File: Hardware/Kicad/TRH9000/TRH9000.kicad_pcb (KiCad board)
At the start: 4 copper layers, 99.1 x 66.6 mm, 89 parts, among them J1 Norcomp_200-015-263R001, J2 Console5_SCART, Q1 BC817, U1 V9990, U2 KM428C256, U3 KM428C256, U4 74VHC138, U5 T.I_SN74AHCT32D, U6 LMH1980, X1 Crystek_CE3291, Y1 Y_HCM4921477270ABJT

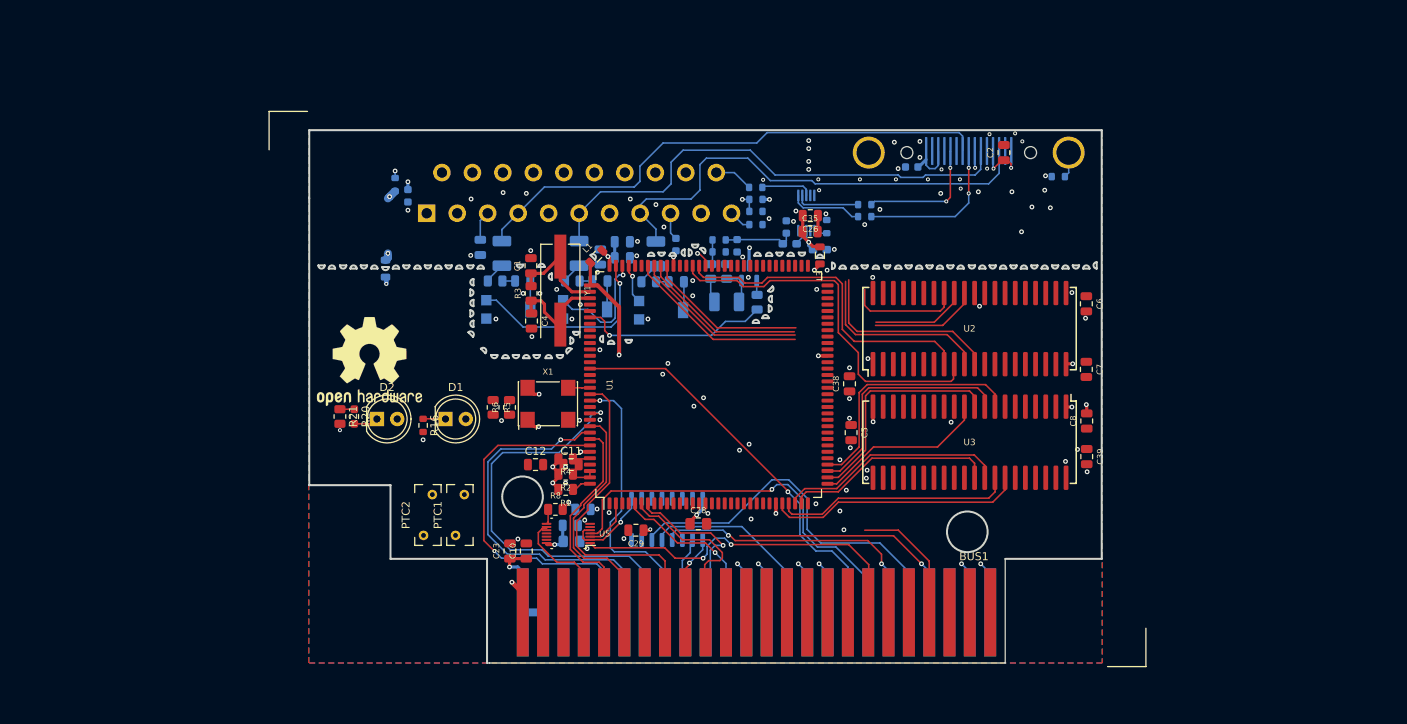
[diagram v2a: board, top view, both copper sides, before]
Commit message: Did a reroute of the analog / digital separation.
Did a reroute of the analog / digital separation.
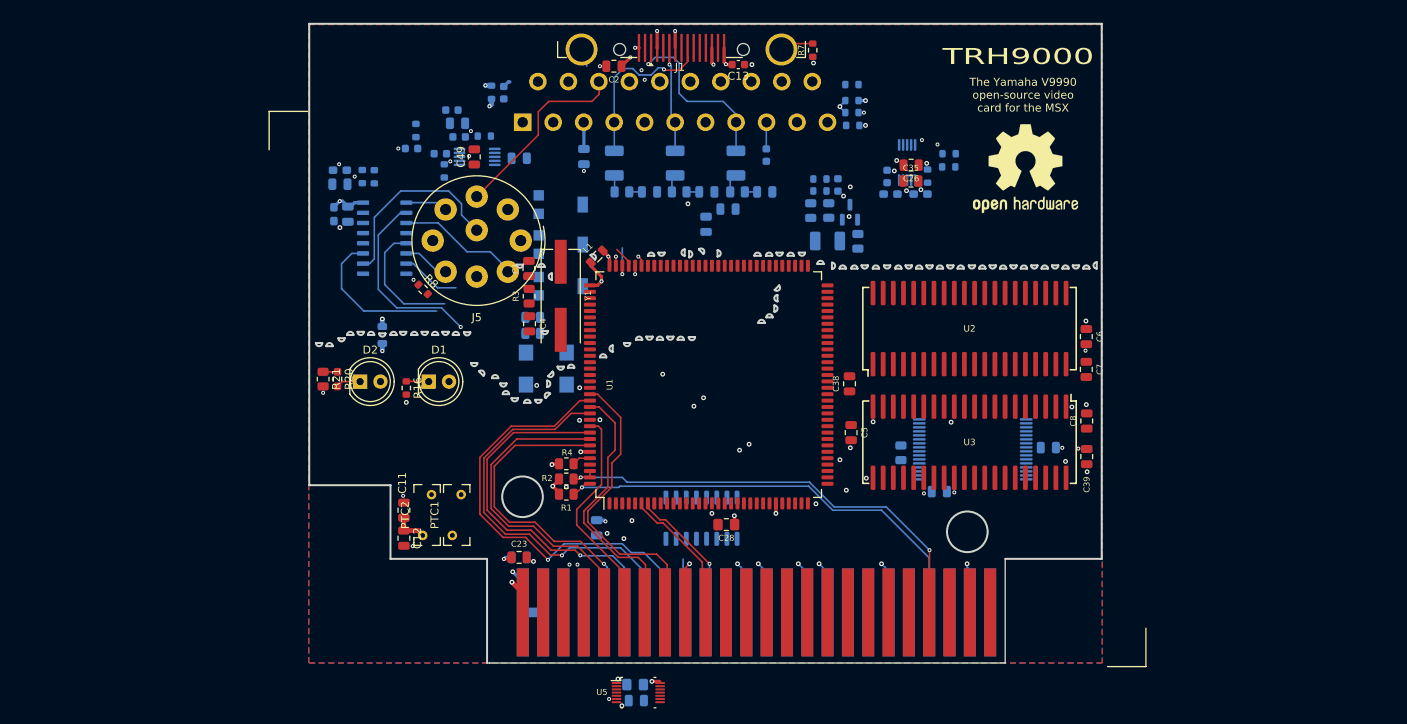
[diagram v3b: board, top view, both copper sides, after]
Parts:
- removed L3: L_MLZ2012M4R7HT000, Inductor_SMD:L_0805_2012Metric
- added C18: C_CL10B104KB8NNNL, Capacitor_SMD:C_0603_1608Metric_Pad1.08x0.95mm_HandSolder, B.Cu at (101.3, 70.9)
- added C22: 47pF, Capacitor_SMD:C_0603_1608Metric, B.Cu at (117.0, 61.2)
- added C41: C_CC0805JPX7R9BB104, Capacitor_SMD:C_0805_2012Metric, B.Cu at (116.8, 59.5)
- added C42: 47pF, Capacitor_SMD:C_0603_1608Metric, B.Cu at (111.0, 62.7)
- added C43: 47pF, LRJ:C_0603_1608Metric_round_court, B.Cu at (116.1, 57.9)
- added C44: C_CL10B104KB8NNNL, LRJ:C_0603_1608Metric_round_court, B.Cu at (114.7, 63.3)
- added C45: C_CL21B106KOQNNNE, Capacitor_SMD:C_0805_2012Metric, B.Cu at (190.7, 100.1)
- added C46: C_CC0805JPX7R9BB104, Capacitor_SMD:C_0805_2012Metric, B.Cu at (177.0, 105.6)
- added C47: C_CL21B106KOQNNNE, Capacitor_SMD:C_0805_2012Metric, B.Cu at (102.1, 67.2)
- added C48: C_CL10B104KB8NNNL, Capacitor_SMD:C_0603_1608Metric_Pad1.08x0.95mm_HandSolder, B.Cu at (102.1, 65.4)
- added C49: 10nF, Capacitor_SMD:C_0805_2012Metric, F.Cu at (118.9, 63.7)
- added J5: DIN-8_SD-80BV, LRJ:Jack_DIN_CUI_SD-80BV_Vertical, F.Cu at (119.2, 74.2)
- added R22: 75, Resistor_SMD:R_0603_1608Metric, B.Cu at (120.2, 61.1)
- added R23: 100, LRJ:R_0603_1608Metric_roundcourt, B.Cu at (111.6, 60.4)
- added R30: R_RC0603FR-0710KL, LRJ:R_0603_1608Metric_roundcourt, B.Cu at (115.2, 65.5)
- added R31: 100, Resistor_SMD:R_0603_1608Metric, B.Cu at (106.4, 66.2)
- added R32: 100, Resistor_SMD:R_0603_1608Metric, B.Cu at (104.9, 66.2)
- added R34: 4K7, Resistor_SMD:R_0805_2012Metric, B.Cu at (172.2, 100.7)
- added U7: T.I_SN74CBT3257, trh9000:Texas_R-PDSO-G16_3.9x9.9mm, B.Cu at (107.7, 73.9)
- added U8: LMH1980, Package_SO:VSSOP-10_3x3mm_P0.5mm, B.Cu at (119.2, 63.7)
- added U9: SST39SF010A-lrj, Package_SO:TSOP-I-32_12.4x8mm_P0.5mm, B.Cu at (181.2, 100.3)
- C10, C29, R5, R6, X1: moved to B.Cu
- C13, J1, R7: moved to F.Cu
- C9: value 47pF -> C_CL21B106KOQNNNE
- R8: value 2K2 -> R_ERJ-3GEYJ105V; footprint Resistor_SMD:R_0805_2012Metric -> Resistor_SMD:R_0603_1608Metric
- moved LOGO1 85.5 mm to (187.8, 65.2)
- moved C2 49.9 mm to (136.3, 52.4), turned to 180 degrees
- moved C9 47.2 mm to (103.1, 70.9), turned to -90 degrees
- moved J1 38.1 mm to (144.8, 46.9), turned to 180 degrees
- moved R7 34.5 mm to (161.2, 50.4), turned to 90 degrees
- moved R8 32.1 mm to (112.5, 80.3), turned to -45 degrees
- moved C13 25.2 mm to (151.9, 52.2), turned to 180 degrees
- moved C31 23.4 mm to (139.2, 131.7), turned to 180 degrees
- moved U5 21.7 mm to (139.4, 130.7), turned to 0 degrees
- moved C11 21.7 mm to (110.1, 107.9), turned to 90 degrees
- moved C30 19.6 mm to (139.0, 129.7), turned to 180 degrees
- moved C16 19.4 mm to (140.8, 68.1)
- moved R19 19.4 mm to (137.3, 68.1)
- moved C12 18.8 mm to (110.1, 111.4), turned to -90 degrees
- moved RV1 18.2 mm to (129.7, 69.7)
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- renumbered C37 to locked
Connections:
- net /VDP/HRESET renamed /V9958_HSYNC
- net /VDP/VRESET renamed /V9958_VSYNC
- net /VDP/~{CSYNC} renamed /VDP/~{CSYNCi}
- net /VIDEO/REXT renamed /VIDEO/REXTi
- BUS1 pad 1: /~{CS1} -> unconnected-(BUS1-Pad1)
- BUS1 pad 12: /~{MERQ} -> unconnected-(BUS1-Pad12)
- BUS1 pad 2: /~{CS2} -> unconnected-(BUS1-Pad2)
- BUS1 pad 42: /SYS_CLK -> unconnected-(BUS1-Pad42)
- C9 pad 1: Net-(C9-Pad1) -> +5VA
- J2 pad 6: unconnected-(J2-Pad6) -> /SOUNDOUT
- R5 pad 1: +5VP -> +5VA
- R6 pad 2: +5VP -> +5VA
- R8 pad 1: Net-(C9-Pad1) -> GND
- R8 pad 2: /SCIN -> Net-(J5-PadSH)
- RV1 pad 3: /VDP/R -> /VIDEO/Rm
- RV2 pad 3: /VDP/G -> /VIDEO/Gm
- RV3 pad 3: /VDP/B -> /VIDEO/Bm
- U1 pad 10: unconnected-(U1-Pad10) -> /VDP/KA15
- U1 pad 11: unconnected-(U1-Pad11) -> /VDP/KA14
- U1 pad 12: unconnected-(U1-Pad12) -> /VDP/KA13
- U1 pad 13: unconnected-(U1-Pad13) -> /VDP/KA12
- U1 pad 14: unconnected-(U1-Pad14) -> /VDP/KA11
- U1 pad 15: unconnected-(U1-Pad15) -> /VDP/KA10
- U1 pad 16: unconnected-(U1-Pad16) -> /VDP/KA9
- U1 pad 37: unconnected-(U1-Pad37) -> /VDP/~{KOE}
- U1 pad 9: unconnected-(U1-Pad9) -> /VDP/KA16
- U1 pad 91: unconnected-(U1-Pad91) -> /VDP/~{YSi}
- U1 pad 93: /VDP/R -> /VDP/Ri
- U1 pad 94: /VDP/G -> /VDP/Gi
- U1 pad 95: /VDP/B -> /VDP/Bi
- U5 pad 10: /SYS_CLK -> unconnected-(U5-Pad10)
- U5 pad 8: /SCIN -> unconnected-(U5-Pad8)
- U5 pad 9: /SYS_CLK -> unconnected-(U5-Pad9)
- X1 pad 1: +5VP -> +5VA
- X1 pad 4: +5VP -> +5VA
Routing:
- net /~{WR}: track 50.8 -> 0.00 mm, vias 1 -> 0
- net /~{RESET}: track 50.5 -> 0.00 mm, vias 1 -> 0
- net /VIDEO/GOUT: track 62.7 -> 13.2 mm, vias 0 -> 1
- net /VDP/V1D1: track 48.3 -> 0.00 mm
- net /~{M1}: track 47.7 -> 0.00 mm
- net /VIDEO/BOUT: track 67.2 -> 20.7 mm, vias 0 -> 1
- net /~{RD}: track 44.6 -> 0.00 mm, vias 2 -> 0
- net /VDP/V1D0: track 41.1 -> 0.00 mm
- net /~{INT}: track 21.3 -> 58.1 mm, vias 0 -> 2
- net /VDP/V1D6: track 36.0 -> 0.00 mm
- net /VIDEO/ROUT: track 59.2 -> 23.2 mm, vias 0 -> 1
- net /D2: track 0.00 -> 34.0 mm
- net /VDP/V1D4: track 33.8 -> 0.00 mm
- net /VDP/V0D7: track 33.4 -> 0.00 mm
- net /VDP/V1D5: track 32.9 -> 0.00 mm
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- added copper zone on In1.Cu, net /VIDEO/GNDD
- added copper zone on In1.Cu, net /VIDEO/VGA_GND
- removed copper zone on In1.Cu, net /VIDEO/AUGND
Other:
- board size 99.1 x 66.6 mm -> 99.1 x 79.9 mm
- board text added: "TRH9000"
- board text removed: "TRH900"

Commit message: Restarted routing from scratch.
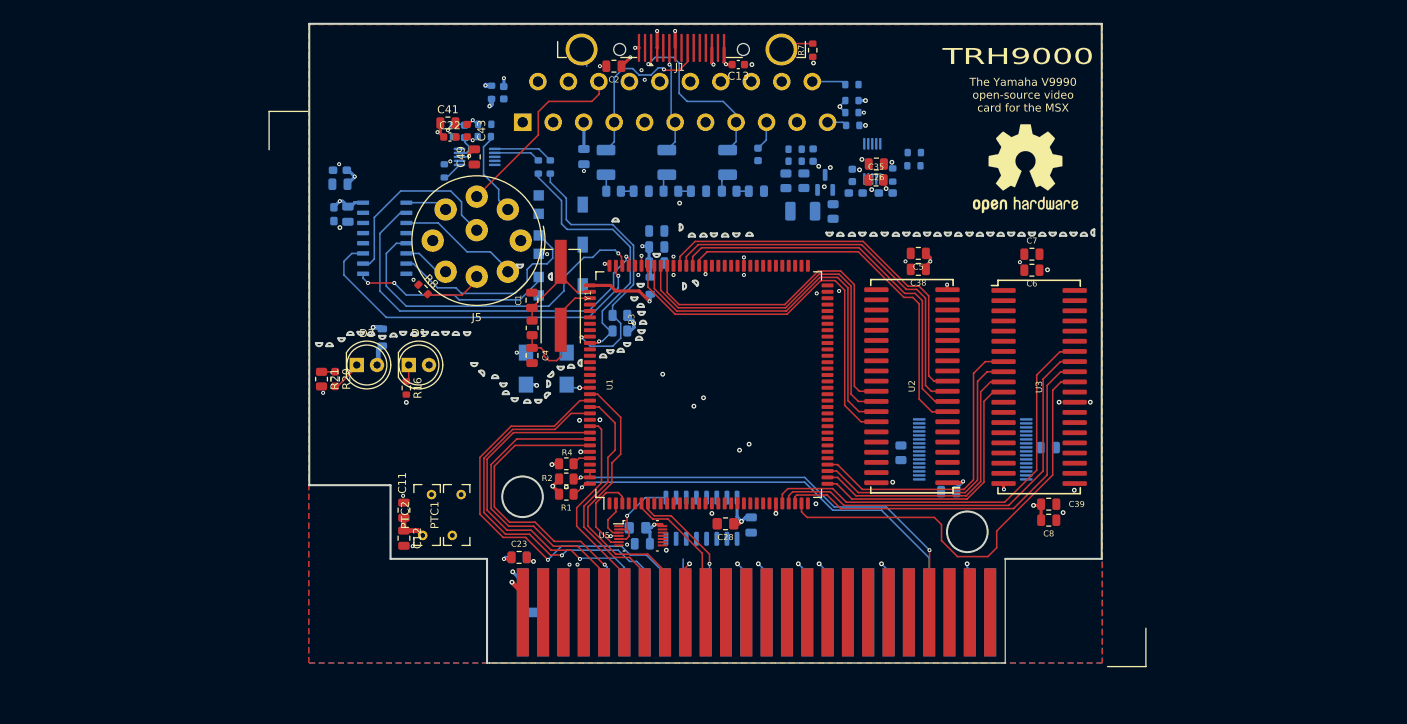
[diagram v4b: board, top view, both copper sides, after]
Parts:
- C22, C41, C43: moved to F.Cu
- L1: moved to B.Cu
- moved C5 23.9 mm to (174.4, 75.8), turned to 180 degrees
- moved R31 22.0 mm to (128.4, 65.0)
- moved R32 22.0 mm to (126.9, 65.0)
- moved C3 21.6 mm to (141.7, 77.0)
- moved C31 19.6 mm to (139.9, 112.1)
- moved C30 19.6 mm to (139.3, 110.1)
- moved U5 19.6 mm to (139.7, 111.1)
- moved C29 19.3 mm to (153.5, 109.8)
- moved C38 16.7 mm to (174.4, 77.8), turned to 180 degrees
- moved C7 15.9 mm to (188.6, 75.9), turned to 0 degrees
- moved C8 13.3 mm to (190.7, 109.2), turned to 180 degrees
- moved U3 11.1 mm to (189.5, 92.5), turned to 0 degrees
- moved R6 10.9 mm to (137.1, 85.5), turned to 0 degrees
- moved R5 10.9 mm to (137.1, 83.5), turned to 180 degrees
- moved C6 10.7 mm to (188.6, 77.9), turned to 180 degrees
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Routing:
- net /VDP/V0D4: track 0.00 -> 55.2 mm
- net /VDP/V0D7: track 0.00 -> 53.5 mm
- net /VDP/V0D6: track 0.00 -> 51.8 mm
- net /VDP/V0D5: track 0.00 -> 50.2 mm
- net /VDP/V1D7: track 0.00 -> 50.1 mm
- net /VDP/V1D6: track 0.00 -> 48.7 mm
- net /VDP/V1D3: track 0.00 -> 48.5 mm
- net /VDP/V1D2: track 0.00 -> 48.4 mm
- net /VDP/V1D1: track 0.00 -> 47.8 mm
- net /VDP/V1D0: track 0.00 -> 47.5 mm
- net /VDP/V1D5: track 0.00 -> 47.3 mm
- net /VDP/V1D4: track 0.00 -> 45.5 mm
- net /VDP/V0D0: track 0.00 -> 37.7 mm
- net /VDP/V0D1: track 0.00 -> 36.6 mm
- net /V9958_HSYNC: track 0.00 -> 36.3 mm, vias 0 -> 1
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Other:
- outline, holes or cut-outs redrawn

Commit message: Further routing, analog is almost complete.
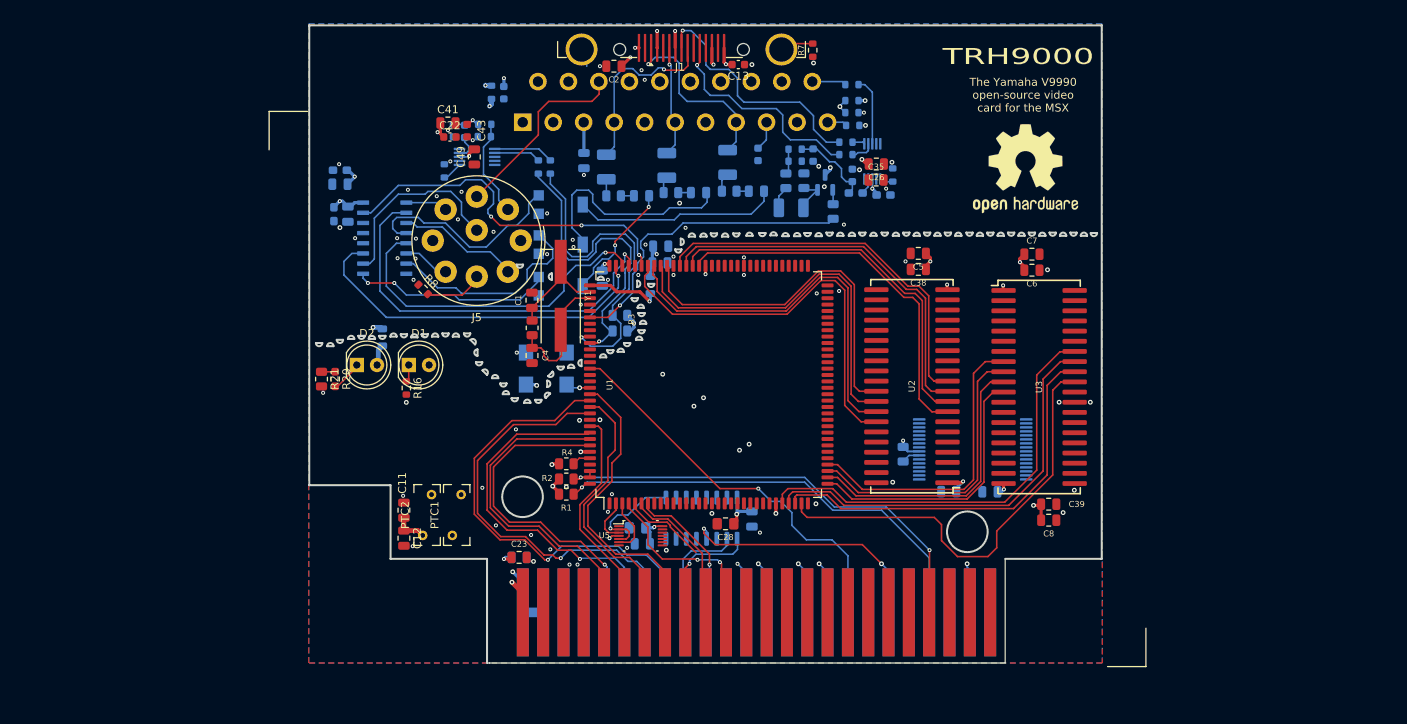
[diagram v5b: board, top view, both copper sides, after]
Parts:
- moved C45 9.16 mm to (183.3, 105.6)
- moved locked 9.00 mm to (134.9, 78.9), turned to -90 degrees
- moved R25 9.00 mm to (165.3, 61.9), turned to 0 degrees
- moved R26 8.55 mm to (165.3, 63.5), turned to 0 degrees
- moved C17 1.51 mm to (158.5, 70.1)
- moved C29 0.76 mm to (153.6, 109.0)
- moved C21 0.58 mm to (135.4, 65.0)
- moved C16 0.58 mm to (139.8, 68.6)
- moved R19 0.57 mm to (136.3, 68.6)
- moved C27 0.51 mm to (142.2, 74.9)
- moved C24 0.50 mm to (132.6, 64.2)
- moved C3 0.40 mm to (142.1, 77.0)
- moved C20 0.38 mm to (143.0, 64.8)
- moved C36 0.37 mm to (170.1, 68.5)
- moved R34 0.33 mm to (172.5, 100.9)
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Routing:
- net /~{RESET}: track 0.00 -> 50.0 mm, vias 0 -> 1
- net /VDP/~{YSi}: track 1.25 -> 45.2 mm, vias 1 -> 3
- net /VDP/~{CSYNCi}: track 0.00 -> 39.0 mm, vias 0 -> 1
- net /VIDEO/HSYNC: track 0.00 -> 31.3 mm, vias 0 -> 1
- net /VIDEO/GIN: track 0.00 -> 27.6 mm
- net /VIDEO/VSYNC: track 0.00 -> 27.2 mm, vias 0 -> 1
- net /VIDEO/Rm: track 0.00 -> 26.2 mm
- net /~{IORQ}: track 6.44 -> 32.2 mm, vias 1 -> 2
- net /VIDEO/RIN: track 0.00 -> 25.7 mm
- net /A0: track 0.00 -> 22.6 mm, vias 0 -> 2
- net /VIDEO/BIN: track 0.00 -> 15.2 mm, vias 0 -> 2
- net /A1: track 0.00 -> 10.6 mm
- net Net-(C32-Pad1): track 0.00 -> 10.3 mm
- net /VIDEO/CSOUT: track 0.00 -> 8.57 mm
- net /A4: track 6.29 -> 14.6 mm
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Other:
- board size 99.1 x 79.9 mm -> 99.1 x 79.7 mm
